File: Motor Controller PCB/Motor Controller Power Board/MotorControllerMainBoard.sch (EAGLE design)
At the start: 50 parts, among them U1 CDBA340L-G

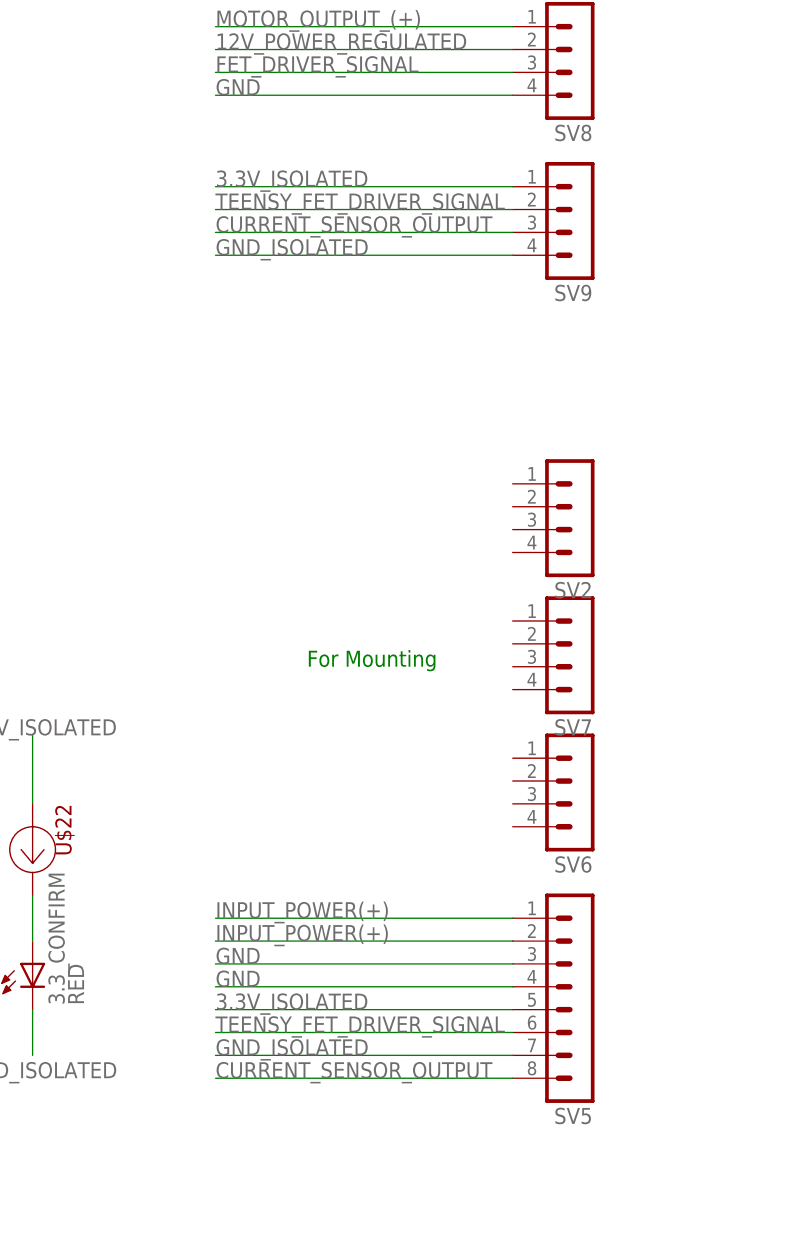
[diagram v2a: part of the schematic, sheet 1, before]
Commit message: Changed connections to logic board
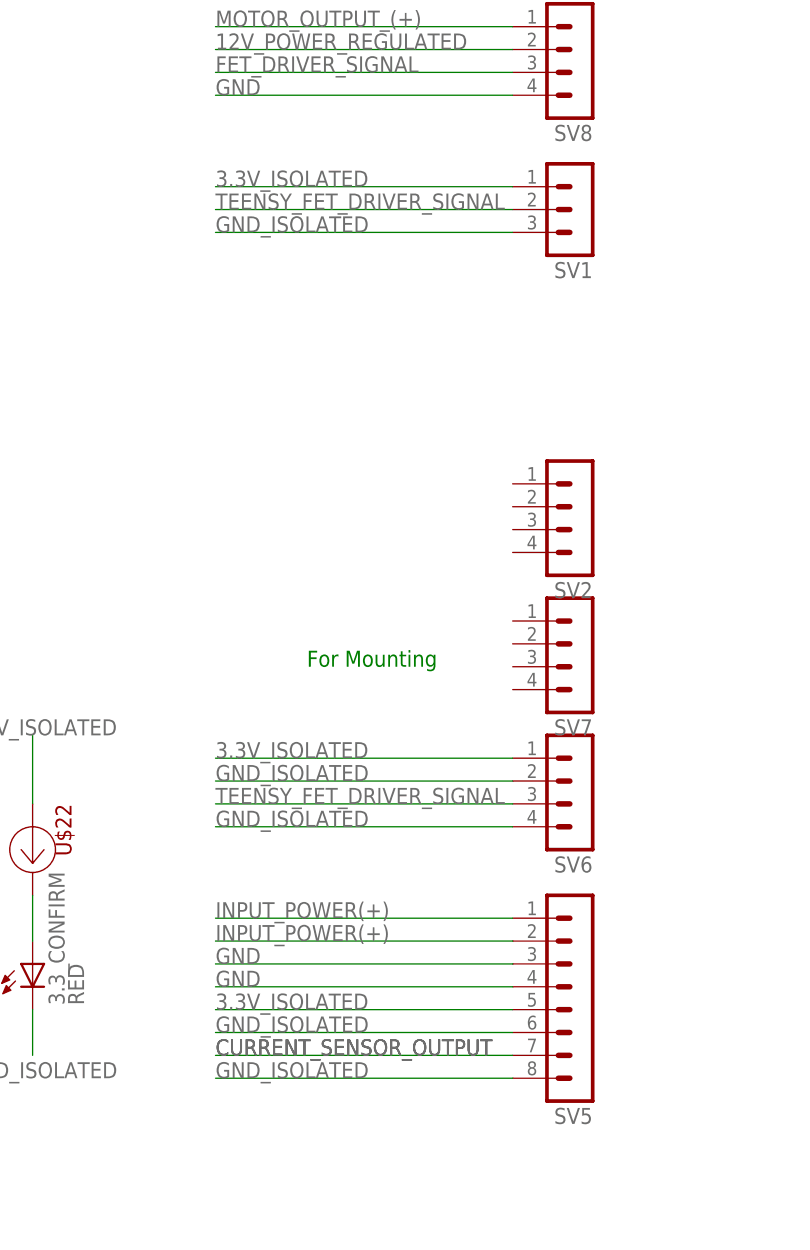
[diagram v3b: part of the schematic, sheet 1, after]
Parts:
- removed SV9: (no value), con-lstb:MA04-1
- added SV1: (no value), con-lstb:MA03-1
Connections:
- net 3.3V_ISOLATED: now also SV1.1, SV6.1; no longer SV9.1
- net CURRENT_SENSOR_OUTPUT: now also SV5.7; no longer SV5.8, SV9.3
- net GND_ISOLATED: now also SV1.3, SV5.6, SV5.8, SV6.2, SV6.4; no longer SV5.7, SV9.4
- net TEENSY_FET_DRIVER_SIGNAL: now also SV1.2, SV6.3; no longer SV5.6, SV9.2
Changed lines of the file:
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@@
 <part name="SV7" library="con-lstb" library_urn="urn:adsk.eagle:library:162" deviceset="MA04-1" device="" package3d_urn="urn:adsk.eagle:package:8337/1"/>
 <part name="SV8" library="con-lstb" library_urn="urn:adsk.eagle:library:162" deviceset="MA04-1" device="" package3d_urn="urn:adsk.eagle:package:8337/1"/>
-<part name="SV9" library="con-lstb" library_urn="urn:adsk.eagle:library:162" deviceset="MA04-1" device="" package3d_urn="urn:adsk.eagle:package:8337/1"/>
 <part name="U$22" library="MotorControllerEagleLibrary" deviceset="AL5809-20S1-7" device=""/>
 <part name="3.3_CONFIRM" library="led" library_urn="urn:adsk.eagle:library:259" deviceset="LED" device="CHIPLED_1206" package3d_urn="urn:adsk.eagle:package:15823/2" value="RED"/>
@@
 <part name="U$25" library="MotorControllerEagleLibrary" deviceset="LTN20069" device=""/>
 <part name="U$24" library="MotorControllerEagleLibrary" deviceset="DA-T263-101E" device=""/>
+<part name="SV1" library="con-lstb" library_urn="urn:adsk.eagle:library:162" deviceset="MA03-1" device="" package3d_urn="urn:adsk.eagle:package:8339/1"/>
 </parts>
 <sheets>
@@
 <instance part="SV7" gate="1" x="266.7" y="121.92" rot="R180"/>
 <instance part="SV8" gate="1" x="266.7" y="187.96" rot="R180"/>
-<instance part="SV9" gate="1" x="266.7" y="170.18" rot="R180"/>
 <instance part="U$22" gate="G$1" x="205.74" y="101.6" rot="R180"/>
 <instance part="3.3_CONFIRM" gate="G$1" x="205.74" y="88.9"/>
 <instance part="U$23" gate="G$1" x="35.56" y="144.78"/>
 <instance part="SV2" gate="1" x="266.7" y="137.16" rot="R180"/>
+<instance part="SV1" gate="G$1" x="266.7" y="172.72" rot="R180"/>
 </instances>
 <busses>
@@
 </segment>
 <segment>
-<wire x1="226.06" y1="81.28" x2="259.08" y2="81.28" width="0.1524" layer="91"/>
-<pinref part="SV5" gate="1" pin="6"/>
-<label x="226.06" y="81.28" size="1.778" layer="95"/>
-</segment>
-<segment>
-<pinref part="SV9" gate="1" pin="2"/>
 <wire x1="259.08" y1="172.72" x2="226.06" y2="172.72" width="0.1524" layer="91"/>
 <label x="226.06" y="172.72" size="1.778" layer="95"/>
+<pinref part="SV1" gate="G$1" pin="2"/>
+</segment>
+<segment>
+<pinref part="SV6" gate="1" pin="3"/>
+<wire x1="259.08" y1="106.68" x2="226.06" y2="106.68" width="0.1524" layer="91"/>
+<label x="226.06" y="106.68" size="1.778" layer="95"/>
 </segment>
 </net>
@@
 <net name="GND_ISOLATED" class="0">
 <segment>
+<wire x1="259.08" y1="170.18" x2="226.06" y2="170.18" width="0.1524" layer="91"/>
+<label x="226.06" y="170.18" size="1.778" layer="95"/>
+<pinref part="SV1" gate="G$1" pin="3"/>
+</segment>
+<segment>
+<pinref part="3.3_CONFIRM" gate="G$1" pin="C"/>
+<wire x1="205.74" y1="83.82" x2="205.74" y2="78.74" width="0.1524" layer="91"/>
+<label x="198.12" y="76.2" size="1.778" layer="95"/>
+</segment>
+<segment>
+<wire x1="226.06" y1="81.28" x2="259.08" y2="81.28" width="0.1524" layer="91"/>
+<pinref part="SV5" gate="1" pin="6"/>
+<label x="226.06" y="81.28" size="1.778" layer="95"/>
+</segment>
+<segment>
+<pinref part="SV5" gate="1" pin="8"/>
+<wire x1="259.08" y1="76.2" x2="226.06" y2="76.2" width="0.1524" layer="91"/>
+<label x="226.06" y="76.2" size="1.778" layer="95"/>
+</segment>
+<segment>
+<pinref part="SV6" gate="1" pin="4"/>
+<wire x1="259.08" y1="104.14" x2="226.06" y2="104.14" width="0.1524" layer="91"/>
+<label x="226.06" y="104.14" size="1.778" layer="95"/>
+</segment>
+<segment>
+<pinref part="SV6" gate="1" pin="2"/>
+<wire x1="259.08" y1="109.22" x2="226.06" y2="109.22" width="0.1524" layer="91"/>
+<label x="226.06" y="109.22" size="1.778" layer="95"/>
+</segment>
+</net>
+<net name="3.3V_ISOLATED" class="0">
+<segment>
+<wire x1="259.08" y1="83.82" x2="226.06" y2="83.82" width="0.1524" layer="91"/>
+<pinref part="SV5" gate="1" pin="5"/>
+<label x="226.06" y="83.82" size="1.778" layer="95"/>
+</segment>
+<segment>
+<wire x1="259.08" y1="175.26" x2="226.06" y2="175.26" width="0.1524" layer="91"/>
+<label x="226.06" y="175.26" size="1.778" layer="95"/>
+<pinref part="SV1" gate="G$1" pin="1"/>
+</segment>
+<segment>
+<wire x1="205.74" y1="114.3" x2="205.74" y2="106.68" width="0.1524" layer="91"/>
+<pinref part="U$22" gate="G$1" pin="A"/>
+<label x="198.12" y="114.3" size="1.778" layer="95"/>
+</segment>
+<segment>
+<pinref part="SV6" gate="1" pin="1"/>
+<wire x1="259.08" y1="111.76" x2="226.06" y2="111.76" width="0.1524" layer="91"/>
+<label x="226.06" y="111.76" size="1.778" layer="95"/>
+</segment>
+</net>
+<net name="CURRENT_SENSOR_OUTPUT" class="0">
+<segment>
 <pinref part="SV5" gate="1" pin="7"/>
 <wire x1="259.08" y1="78.74" x2="226.06" y2="78.74" width="0.1524" layer="91"/>
 <label x="226.06" y="78.74" size="1.778" layer="95"/>
-</segment>
-<segment>
-<pinref part="SV9" gate="1" pin="4"/>
-<wire x1="259.08" y1="167.64" x2="226.06" y2="167.64" width="0.1524" layer="91"/>
-<label x="226.06" y="167.64" size="1.778" layer="95"/>
-</segment>
-<segment>
-<pinref part="3.3_CONFIRM" gate="G$1" pin="C"/>
-<wire x1="205.74" y1="83.82" x2="205.74" y2="78.74" width="0.1524" layer="91"/>
-<label x="198.12" y="76.2" size="1.778" layer="95"/>
-</segment>
-</net>
-<net name="3.3V_ISOLATED" class="0">
-<segment>
-<wire x1="259.08" y1="83.82" x2="226.06" y2="83.82" width="0.1524" layer="91"/>
-<pinref part="SV5" gate="1" pin="5"/>
-<label x="226.06" y="83.82" size="1.778" layer="95"/>
-</segment>
-<segment>
-<pinref part="SV9" gate="1" pin="1"/>
-<wire x1="259.08" y1="175.26" x2="226.06" y2="175.26" width="0.1524" layer="91"/>
-<label x="226.06" y="175.26" size="1.778" layer="95"/>
-</segment>
-<segment>
-<wire x1="205.74" y1="114.3" x2="205.74" y2="106.68" width="0.1524" layer="91"/>
-<pinref part="U$22" gate="G$1" pin="A"/>
-<label x="198.12" y="114.3" size="1.778" layer="95"/>
-</segment>
-</net>
-<net name="CURRENT_SENSOR_OUTPUT" class="0">
-<segment>
-<pinref part="SV5" gate="1" pin="8"/>
-<wire x1="259.08" y1="76.2" x2="226.06" y2="76.2" width="0.1524" layer="91"/>
-<label x="226.06" y="76.2" size="1.778" layer="95"/>
-</segment>
-<segment>
-<pinref part="SV9" gate="1" pin="3"/>
-<wire x1="259.08" y1="170.18" x2="226.06" y2="170.18" width="0.1524" layer="91"/>
-<label x="226.06" y="170.18" size="1.778" layer="95"/>
-</segment>
-</net>
+<label x="226.06" y="78.74" size="1.778" layer="95"/>
+</segment>
+</net>

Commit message: this is going to be nuked when i change headers
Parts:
- added SV3: (no value), con-lstb:MA04-1
- added U$10: EEU-FM1H102B, MotorControllerEagleLibrary:EEU-FM1H102B
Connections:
- net GND: now also U$10.NEGATIVE
- net INPUT_POWER(+): now also U$10.POSITIVE
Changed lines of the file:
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@@
 <part name="U$24" library="MotorControllerEagleLibrary" deviceset="DA-T263-101E" device=""/>
 <part name="SV1" library="con-lstb" library_urn="urn:adsk.eagle:library:162" deviceset="MA03-1" device="" package3d_urn="urn:adsk.eagle:package:8339/1"/>
+<part name="U$10" library="MotorControllerEagleLibrary" deviceset="EEU-FM1H102B" device=""/>
+<part name="SV3" library="con-lstb" library_urn="urn:adsk.eagle:library:162" deviceset="MA04-1" device="" package3d_urn="urn:adsk.eagle:package:8337/1"/>
 </parts>
 <sheets>
@@
 <instance part="SV2" gate="1" x="266.7" y="137.16" rot="R180"/>
 <instance part="SV1" gate="G$1" x="266.7" y="172.72" rot="R180"/>
+<instance part="SV3" gate="1" x="254" y="137.16" rot="R180"/>
 </instances>
 <busses>
@@
 <instance part="U$18" gate="G$1" x="66.04" y="157.48" rot="R270"/>
 <instance part="U$19" gate="G$1" x="78.74" y="157.48" rot="R270"/>
+<instance part="U$10" gate="G$1" x="88.9" y="157.48" rot="R270"/>
 </instances>
 <busses>
@@
 <pinref part="U$18" gate="G$1" pin="POSITIVE"/>
 <pinref part="U$19" gate="G$1" pin="POSITIVE"/>
+<pinref part="U$10" gate="G$1" pin="POSITIVE"/>
+<wire x1="78.74" y1="160.02" x2="88.9" y2="160.02" width="0.1524" layer="91"/>
+<wire x1="88.9" y1="160.02" x2="88.9" y2="157.48" width="0.1524" layer="91"/>
+<junction x="78.74" y="160.02"/>
 </segment>
 </net>
@@
 <wire x1="53.34" y1="144.78" x2="66.04" y2="144.78" width="0.1524" layer="91"/>
 <wire x1="66.04" y1="144.78" x2="78.74" y2="144.78" width="0.1524" layer="91"/>
-<wire x1="78.74" y1="144.78" x2="96.52" y2="144.78" width="0.1524" layer="91"/>
+<wire x1="78.74" y1="144.78" x2="88.9" y2="144.78" width="0.1524" layer="91"/>
+<wire x1="88.9" y1="144.78" x2="96.52" y2="144.78" width="0.1524" layer="91"/>
 <wire x1="53.34" y1="149.86" x2="53.34" y2="144.78" width="0.1524" layer="91"/>
 <wire x1="66.04" y1="149.86" x2="66.04" y2="144.78" width="0.1524" layer="91"/>
@@
 <pinref part="U$18" gate="G$1" pin="NEGATIVE"/>
 <pinref part="U$19" gate="G$1" pin="NEGATIVE"/>
-</segment>
-<segment>
+<pinref part="U$10" gate="G$1" pin="NEGATIVE"/>
+<wire x1="88.9" y1="149.86" x2="88.9" y2="144.78" width="0.1524" layer="91"/>
+<junction x="88.9" y="144.78"/>
+</segment>
+<segment>

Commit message: Made a layout, need labels
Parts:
- removed C5, C6: EEUFR1H221B, MotorControllerEagleLibrary:EEUFR1H221B
- removed SV2, SV3, SV6, SV7: (no value), con-lstb:MA04-1
- removed SV5: (no value), con-lstb:MA08-1
- removed U$24: DA-T263-101E, MotorControllerEagleLibrary:DA-T263-101E
- removed U$7: 100uH, MotorControllerEagleLibrary:PA4320
- removed U1: CDBA340L-G, MotorControllerEagleLibrary:CDBA340L-G
- added J1: (no value), SparkFun-Connectors:DB9FEMALE
- 3.3_CONFIRM, PWR_CONFIRM: device led:LEDCHIPLED_1206 -> SparkFun-LED:LED-RED1206
- U$12, U$14, U$15, U$16: value 732-3204-ND_CONNECTOR -> 74650073R; device Connector 732-3204:732-3204-ND_CONNECTOR -> MotorControllerEagleLibrary:74650073R
- U$6: value TL2575HV-15IKTTR -> KHHD004A2B; device MotorControllerEagleLibrary:TL2575HV-15IKTTR -> MotorControllerEagleLibrary:KHHD004A2B
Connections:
- removed net N$1: U$6.OUTPUT, U$7.+, U1.11
- removed net POWER_INPUT(+): U$9.5
- new net ENABLE_12V: J1.8, U$6.ON/OFF
- new net N$11: U$6.SENSE(+)
- new net N$5: U$6.SENSE(-)
- new net N$8: U$6.TRIM
- net 12V_POWER_REGULATED: now also J1.2, U$6.VO(+); no longer C5.POSITIVE, C6.POSITIVE, U$6.FEEDBACK, U$7.-
- net 3.3V_ISOLATED: now also J1.1, J1.9; no longer SV5.5, SV6.1
- net CURRENT_SENSOR_OUTPUT: now also J1.5; no longer SV5.7
- net GND: now also J1.7, U$15.P$1, U$6.VI(-), U$6.VO(-); no longer C5.NEGATIVE, C6.NEGATIVE, SV5.3, SV5.4, U$14.P$1, U$24.GND, U$6.!ON/OFF, U$6.EPAD, U$6.GND, U1.22
- net GND_ISOLATED: now also J1.4; no longer SV5.6, SV5.8, SV6.2, SV6.4
- net INPUT_POWER(+): now also J1.3, U$14.P$1, U$6.VI(+), U$9.4; no longer C36.1, C37.1, C38.1, C39.1, C40.1, SV5.1, SV5.2, U$10.POSITIVE, U$12.P$1, U$13.POSITIVE, U$18.POSITIVE, U$19.POSITIVE
- net MOTOR_OUTPUT_(+): now also C36.1, C37.1, C38.1, C39.1, C40.1, U$10.POSITIVE, U$13.POSITIVE, U$16.P$1, U$18.POSITIVE, U$19.POSITIVE, U$9.5; no longer U$15.P$1, U$6.VIN, U$9.4
- net MOTOR_OUTPUT_(--): now also U$12.P$1; no longer U$16.P$1
- net TEENSY_FET_DRIVER_SIGNAL: now also J1.6, U$17.1.ANODE; no longer SV6.3
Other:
- note removed: "2.8A Rating"
- note removed: "220uF Panasonic Caps"
- note removed: "For Mounting"
- note removed: "HeatSink"
